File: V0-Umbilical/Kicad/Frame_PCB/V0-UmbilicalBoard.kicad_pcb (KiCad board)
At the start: 2 copper layers, 122 x 37 mm, 16 parts, among them J1 Conn_02x08_Odd_Even, J10 Neopixel Strip 1, J11 Neopixel Strip 1, J12 Neopixel Out, J2 Motor, J3 Hotend Fan, J4 Part Cooling Fan, J5 Heater, J6 Thermistor, J7 X-Endstop, J8 Chamber Thermistor, J9 Neopixel (from controller)

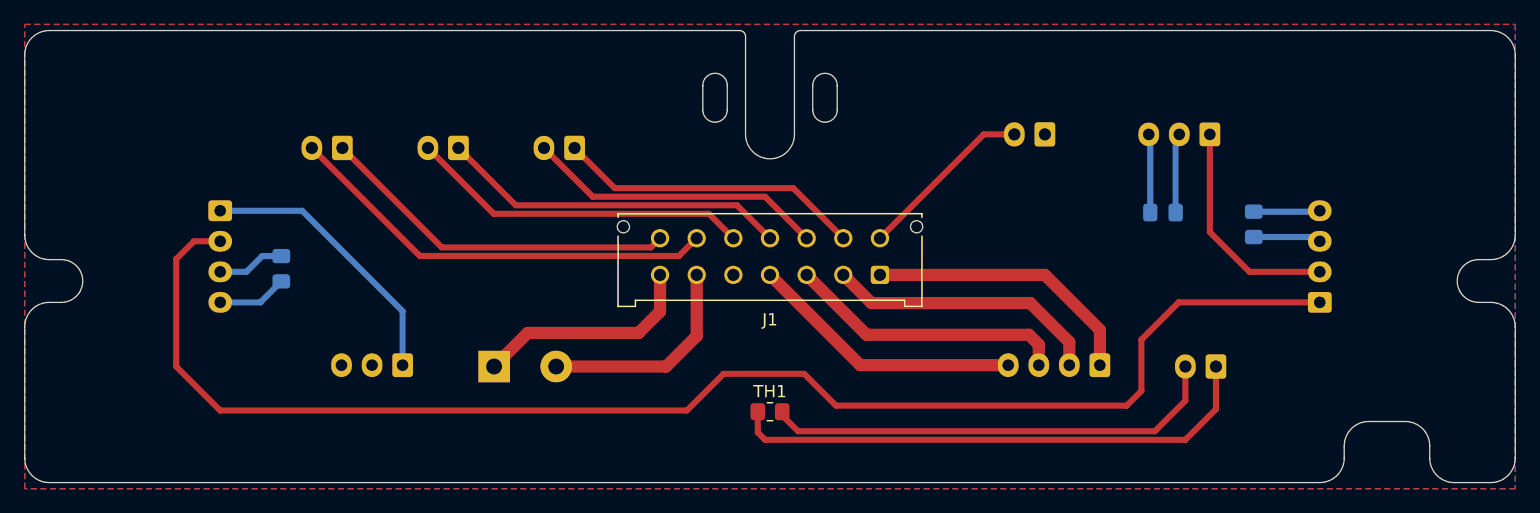
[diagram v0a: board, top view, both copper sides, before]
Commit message: Adding SuperPINDA and exhaust fan connectors.
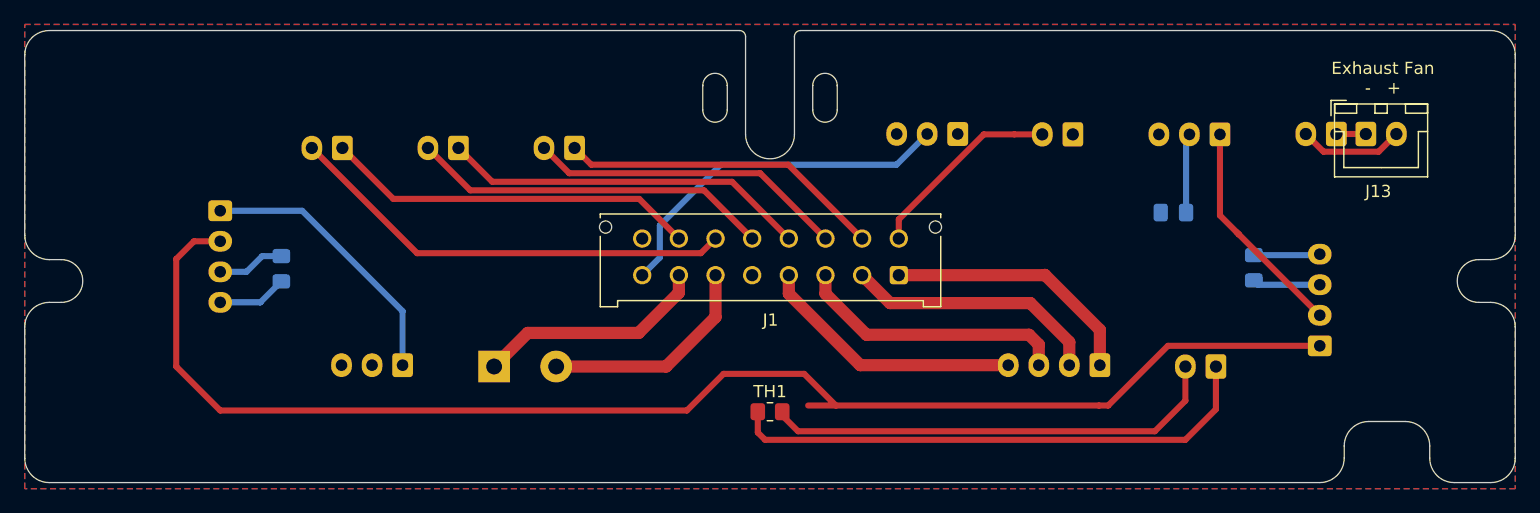
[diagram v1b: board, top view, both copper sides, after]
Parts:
- added J13: Exhaust Fan Out, Connector_JST:JST_XH_B2B-XH-A_1x02_P2.50mm_Vertical, F.Cu at (148.8, 90.0)
- added J14: Exhaust Fan In, Connector_JST:JST_XH_B2B-XH-A_1x02_P2.50mm_Vertical, B.Cu at (146.4, 90.0)
- added J15: SuperPINDA, Connector_JST:JST_XH_B3B-XH-A_1x03_P2.50mm_Vertical, B.Cu at (115.4, 90.0)
- J1: footprint Connector_Molex:Molex_Micro-Fit_3.0_43045-1412_2x07_P3.00mm_Vertical -> Connector_Molex:Molex_Micro-Fit_3.0_43045-1612_2x08_P3.00mm_Vertical
- moved C1 3.56 mm to (139.6, 100.9)
- moved J10 3.56 mm to (145.0, 107.3)
- moved J7 2.29 mm to (124.8, 90.0)
- moved J1 1.54 mm to (110.5, 101.5)
- moved C2 0.86 mm to (133.0, 96.4)
- moved J9 0.83 mm to (136.8, 90.0)
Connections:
- J1 pad 10: /PartFan- -> /PartFan+
- J1 pad 11: /Hotend_Fan- -> /PartFan-
- J1 pad 12: /Hotend_Fan+ -> /Hotend_Fan-
- J1 pad 13: Net-(J1-Pad13) -> /Hotend_Fan+
- J1 pad 8: Net-(J1-Pad8) -> /Z-Endstop
- J1 pad 9: /PartFan+ -> Net-(J1-Pad9)
- J6 pad 1: Net-(J1-Pad14) -> Net-(J1-Pad15)
- J6 pad 2: Net-(J1-Pad13) -> Net-(J1-Pad14)
- J7 pad 2: Net-(J1-Pad8) -> Net-(J1-Pad9)
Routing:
- net Net-(J1-Pad13): track 35.8 -> 0.00 mm
- net Net-(J1-Pad15): track 0.00 -> 30.6 mm
- net /Z-Endstop: track 0.00 -> 29.6 mm
- net Net-(J1-Pad9): track 0.00 -> 16.2 mm
- net Net-(J1-Pad8): track 14.5 -> 0.00 mm
- net /ExhaustFan+: track 0.00 -> 8.61 mm
- net Net-(J1-Pad14): track 29.7 -> 37.1 mm
- net Ground: track 17.6 -> 11.1 mm
- net /ExhaustFan-: track 0.00 -> 2.41 mm
- net DataIn2: track 116.4 -> 114.7 mm
- net /PartFan+: track 25.1 -> 26.6 mm
- net /Hotend_Fan-: track 28.6 -> 30.1 mm
- net /A2: track 22.7 -> 21.1 mm
- net /PartFan-: track 24.6 -> 26.1 mm
- net /Hotend_Fan+: track 28.1 -> 29.6 mm
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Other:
- board text added: "Exhaust Fan - +"
- board text added: "SuperPINDA GND Data 5V"

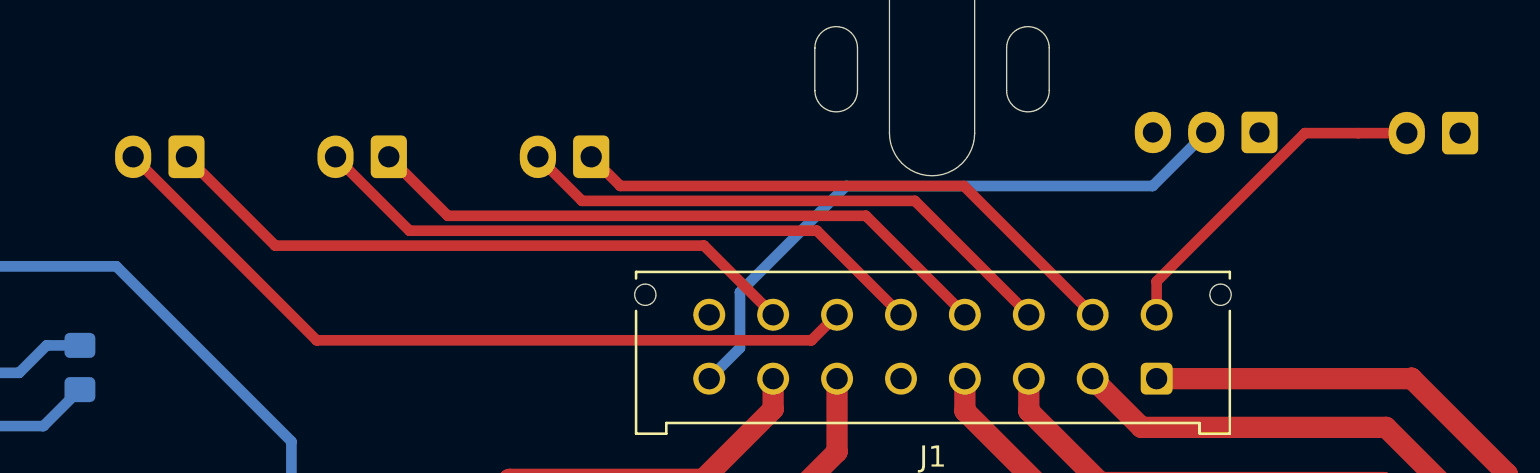
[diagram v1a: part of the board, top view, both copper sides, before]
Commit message: Clean up DRC errors.
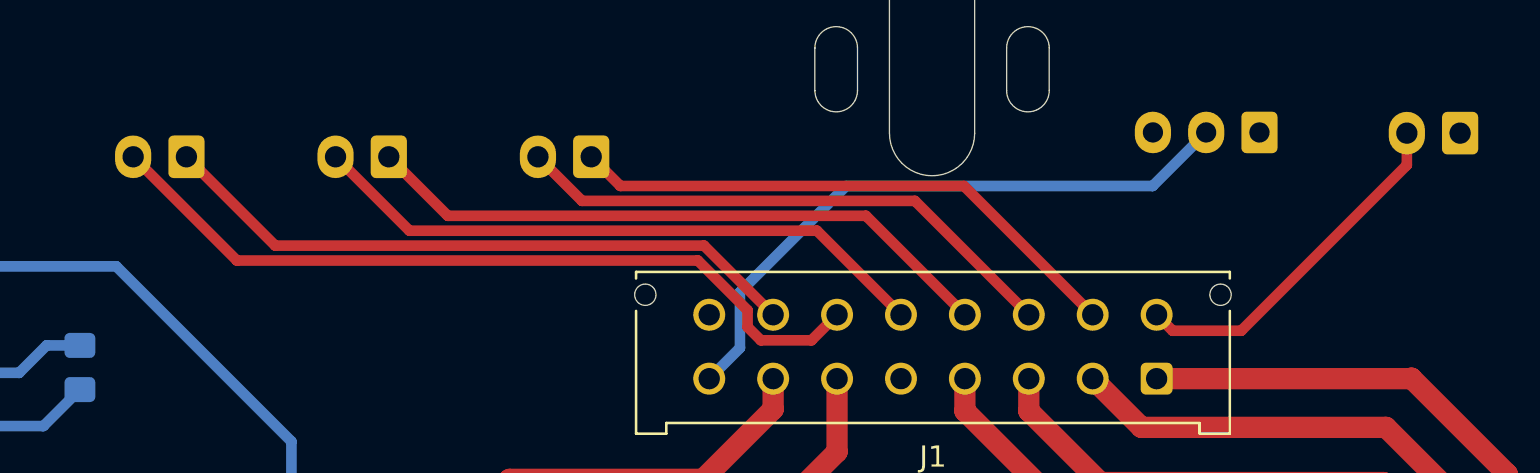
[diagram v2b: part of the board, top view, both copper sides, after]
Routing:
- net Net-(J1-Pad9): track 16.2 -> 16.8 mm

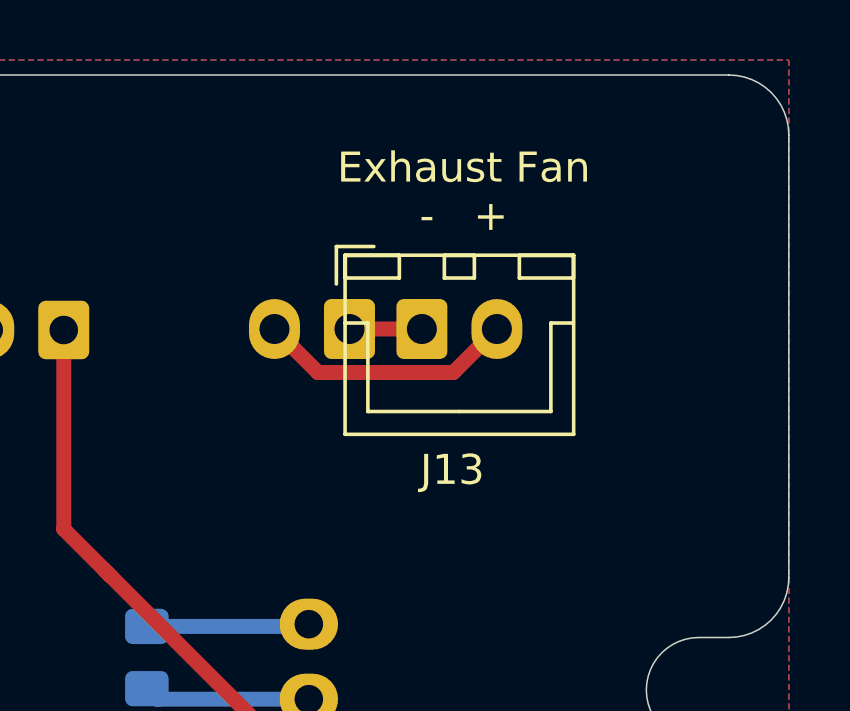
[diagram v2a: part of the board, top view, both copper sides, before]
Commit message: Fixed the exhaust fan headers colliding.
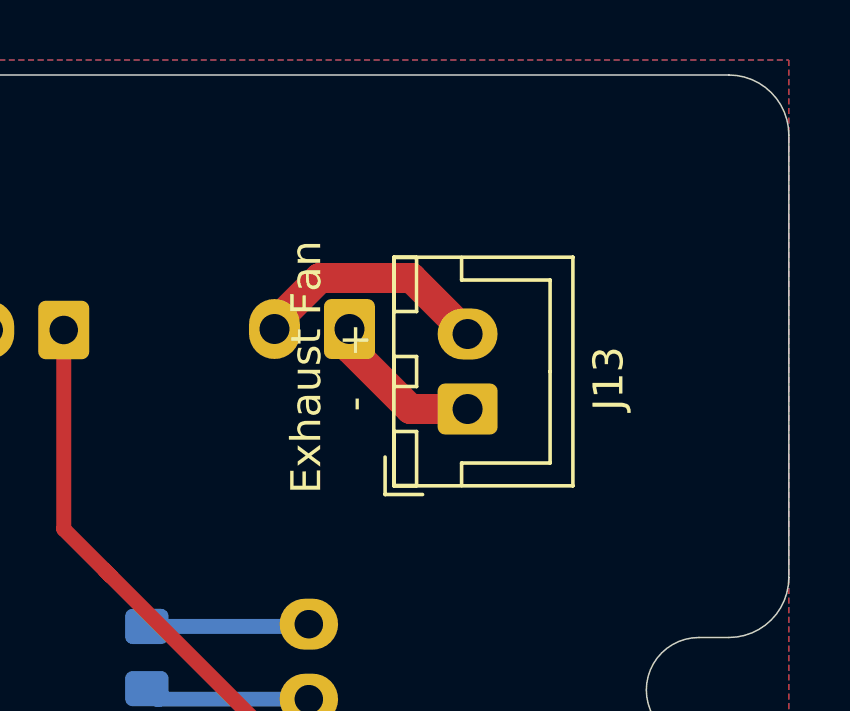
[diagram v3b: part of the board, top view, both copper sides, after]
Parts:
- moved J13 3.07 mm to (150.3, 92.6), turned to 90 degrees
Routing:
- net /ExhaustFan-: track 2.41 -> 5.41 mm
- net /ExhaustFan+: track 8.61 -> 8.03 mm
